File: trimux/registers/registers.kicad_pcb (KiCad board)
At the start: 2 copper layers, 50 x 50 mm, 36 parts, among them P1 CONN_02X05, U1 trimux, U2 trimux, U3 trimux, U4 trimux, U5 trimux, U6 trimux

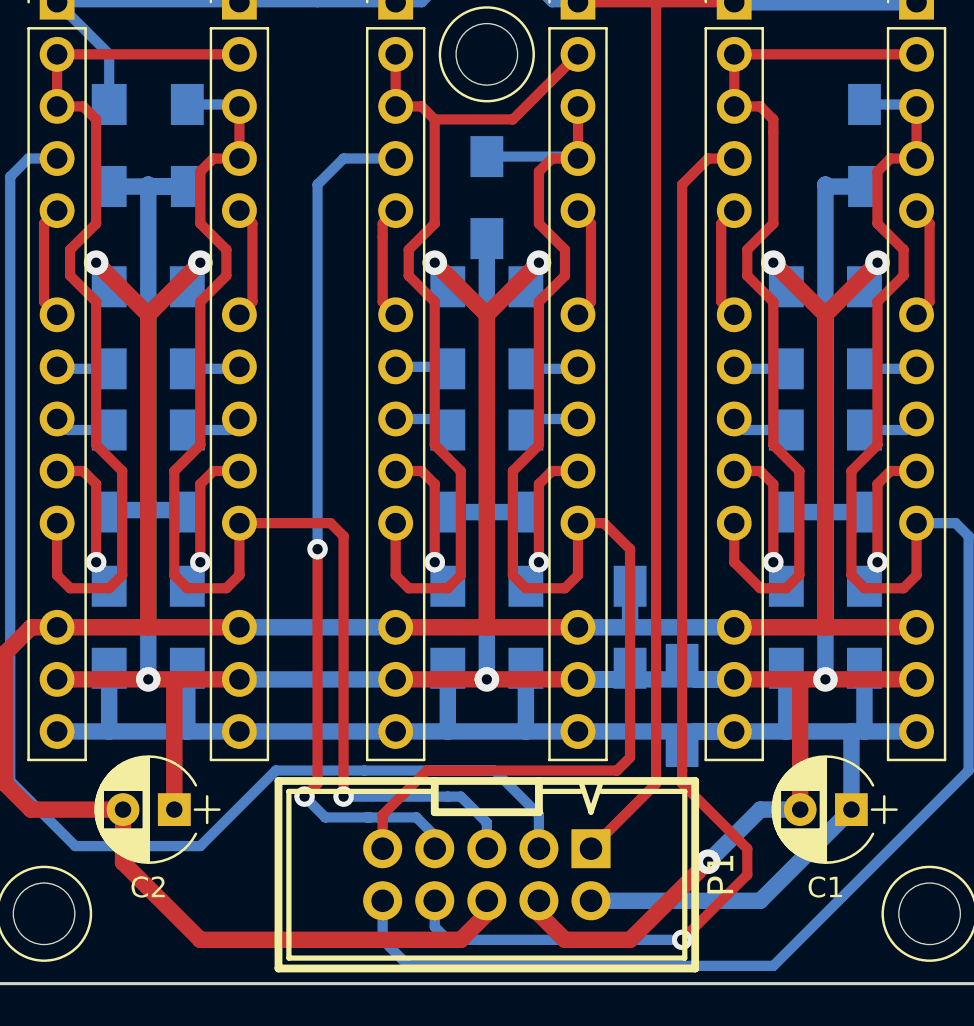
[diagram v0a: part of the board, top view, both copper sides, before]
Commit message: registers silkscreens
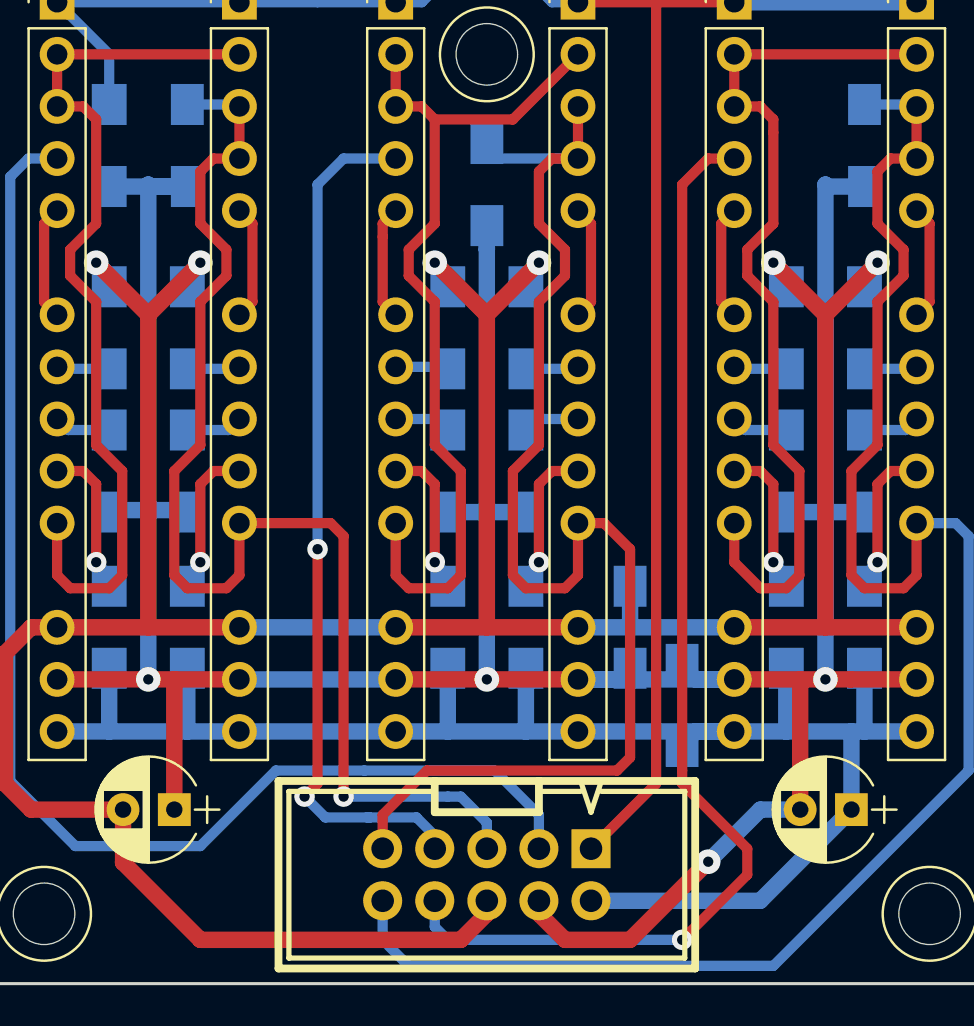
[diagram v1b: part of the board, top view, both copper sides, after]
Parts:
- moved C6 0.64 mm to (40.0, 26.0)
- renumbered REF** to 47uF
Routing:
- net GNDREF: track 166.0 -> 167.2 mm

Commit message: registers
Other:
- board text added: "+5"
- board text added: "-5"
- board text added: "0"
- board text added: "3-trit register"
- board text added: "Ahi"
- board text added: "Alo"
- board text added: "Ami"
- board text added: "CLK"
- board text added: "FlipFlapFlop high"
- board text added: "FlipFlapFlop low"
- board text added: "FlipFlapFlop mid"
- board text added: "Qhi"
- board text added: "Qlo"
- board text added: "Qmi"
- board text added: "this register stores 3-trit value on P-O-N clock fronts"
- board text added: "v25.09.2017"
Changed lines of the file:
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@@
-(kicad_pcb (version 4) (host pcbnew 4.0.5)
+(kicad_pcb (version 4) (host pcbnew 4.0.5+dfsg1-4)
   (general
     (links 103)
@@
     (area 14.924999 14.924999 65.075001 65.075001)
     (thickness 1.6)
-    (drawings 4)
+    (drawings 20)
     (tracks 381)
     (zones 0)
@@
     )
   )
+  (gr_text "this register stores 3-trit value\non P-O-N clock fronts" (at 48.26 34.925 90) (layer F.SilkS)
+    (effects (font (size 1.2 1.2) (thickness 0.2)))
+  )
+  (gr_text v25.09.2017 (at 63.754 21.336 90) (layer B.SilkS)
+    (effects (font (size 1.2 1.2) (thickness 0.3)) (justify mirror))
+  )
+  (gr_text "3-trit\nregister" (at 25.146 61.468) (layer F.SilkS)
+    (effects (font (size 1.2 1.2) (thickness 0.3)))
+  )
+  (gr_text CLK (at 46.99 56.388) (layer B.SilkS)
+    (effects (font (size 1.2 1.2) (thickness 0.3)) (justify mirror))
+  )
+  (gr_text Qhi (at 40.005 55.245) (layer B.SilkS)
+    (effects (font (size 1.2 1.2) (thickness 0.3)) (justify mirror))
+  )
+  (gr_text Ahi (at 42.545 56.515) (layer B.SilkS)
+    (effects (font (size 1.2 1.2) (thickness 0.3)) (justify mirror))
+  )
+  (gr_text Ami (at 36.83 56.515) (layer B.SilkS)
+    (effects (font (size 1.2 1.2) (thickness 0.3)) (justify mirror))
+  )
+  (gr_text Qmi (at 32.258 57.404) (layer B.SilkS)
+    (effects (font (size 1.2 1.2) (thickness 0.3)) (justify mirror))
+  )
+  (gr_text Qlo (at 32.512 62.23) (layer B.SilkS)
+    (effects (font (size 1.2 1.2) (thickness 0.3)) (justify mirror))
+  )
+  (gr_text Alo (at 36.83 62.992) (layer B.SilkS)
+    (effects (font (size 1.2 1.2) (thickness 0.3)) (justify mirror))
+  )
+  (gr_text -5 (at 40.64 62.992) (layer B.SilkS)
+    (effects (font (size 1.2 1.2) (thickness 0.3)) (justify mirror))
+  )
+  (gr_text 0 (at 43.18 62.992) (layer B.SilkS)
+    (effects (font (size 1.2 1.2) (thickness 0.3)) (justify mirror))
+  )
+  (gr_text +5 (at 47.498 62.484) (layer B.SilkS)
+    (effects (font (size 1.2 1.2) (thickness 0.3)) (justify mirror))
+  )
+  (gr_text "FlipFlapFlop mid" (at 40.005 38.1 90) (layer F.SilkS)
+    (effects (font (size 2.5 2.5) (thickness 0.3)))
+  )
+  (gr_text "FlipFlapFlop low" (at 56.515 34.925 90) (layer F.SilkS)
+    (effects (font (size 2.5 2.5) (thickness 0.3)))
+  )
+  (gr_text "FlipFlapFlop high" (at 23.495 34.925 90) (layer F.SilkS)
+    (effects (font (size 2.5 2.5) (thickness 0.3)))
+  )
   (gr_line (start 15 65) (end 15 15) (angle 90) (layer Edge.Cuts) (width 0.15))
   (gr_line (start 65 65) (end 15 65) (angle 90) (layer Edge.Cuts) (width 0.15))
@@
   (segment (start 21.59 52.705) (end 25.4 52.705) (width 0.8) (layer B.Cu) (net 1))
   (segment (start 25.4 52.705) (end 27.94 52.705) (width 0.8) (layer B.Cu) (net 1))
-  (segment (start 40.005 29.21) (end 40.005 28.035) (width 0.8) (layer B.Cu) (net 2) (status 800000))
+  (segment (start 40.005 29.21) (end 40.005 28.035) (width 0.8) (layer B.Cu) (net 2))
   (segment (start 35.56 50.165) (end 27.94 50.165) (width 0.8) (layer B.Cu) (net 2))
   (segment (start 42.545 61.595) (end 43.815 62.865) (width 0.8) (layer F.Cu) (net 2))
@@
   (segment (start 27.305 29.21) (end 27.305 29.21) (width 0.5) (layer F.Cu) (net 4))
   (segment (start 27.94 24.765) (end 27.94 22.225) (width 0.5) (layer F.Cu) (net 4))
-  (segment (start 40.005 24.035) (end 40.005 24.13) (width 0.5) (layer B.Cu) (net 5) (status C00000))
-  (segment (start 40.005 24.13) (end 40.64 24.765) (width 0.5) (layer B.Cu) (net 5) (status C00000))
-  (segment (start 40.64 24.765) (end 44.45 24.765) (width 0.5) (layer B.Cu) (net 5) (status C00000))
+  (segment (start 40.005 24.035) (end 40.005 24.13) (width 0.5) (layer B.Cu) (net 5))
+  (segment (start 40.005 24.13) (end 40.64 24.765) (width 0.5) (layer B.Cu) (net 5))
+  (segment (start 40.64 24.765) (end 44.45 24.765) (width 0.5) (layer B.Cu) (net 5))
   (segment (start 46.99 53.975) (end 46.355 54.61) (width 0.5) (layer F.Cu) (net 5))
   (segment (start 45.72 42.545) (end 46.99 43.815) (width 0.5) (layer F.Cu) (net 5))

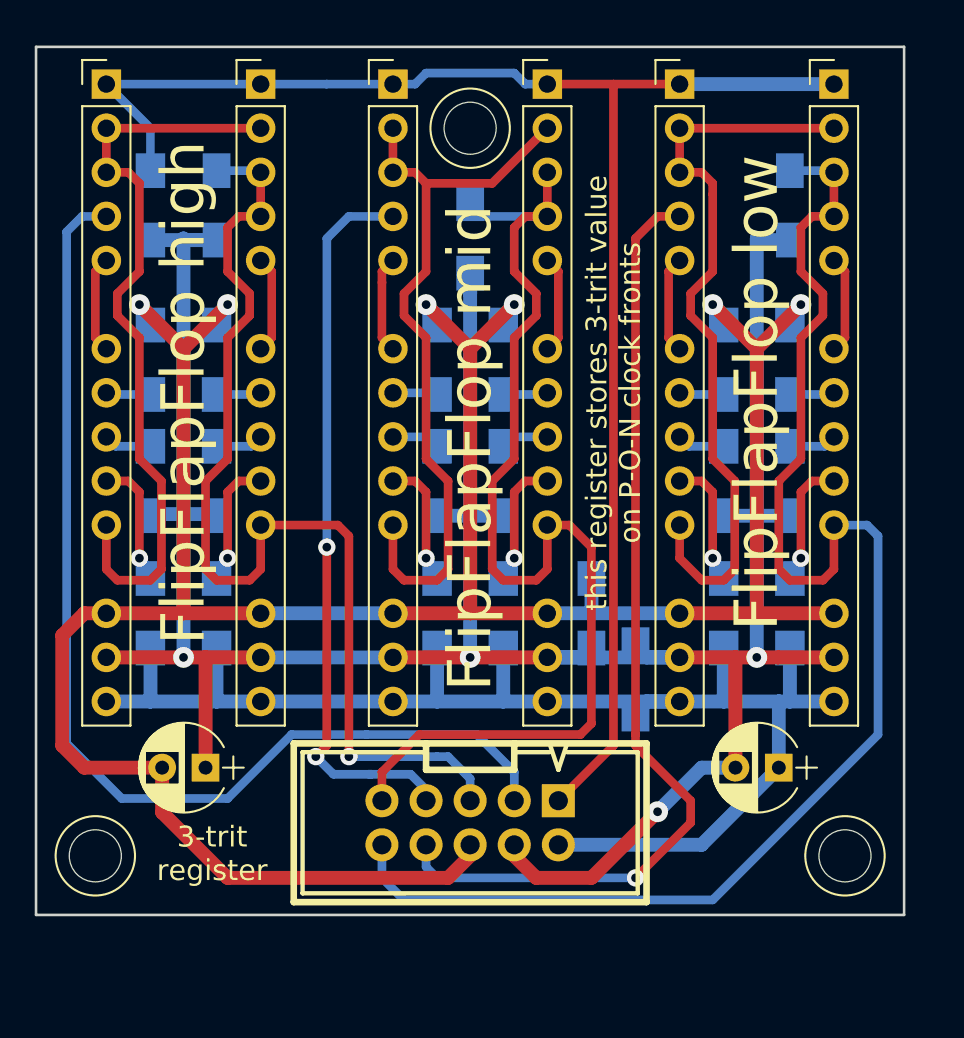
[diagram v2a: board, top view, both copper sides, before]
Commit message: leds for the flipflapflop register
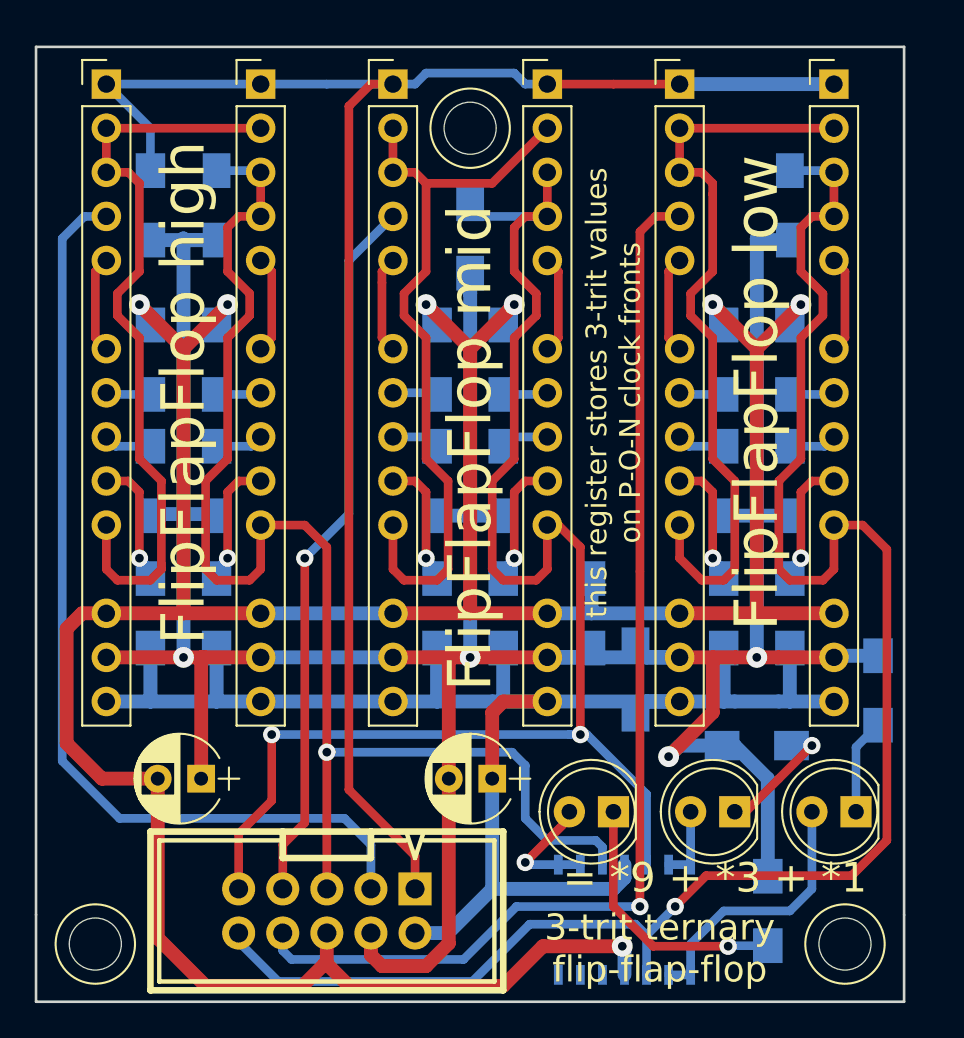
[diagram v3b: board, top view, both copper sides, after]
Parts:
- removed 47uF (x2): 1pin, Connectors:1pin
- added D1: LED_bicolor, LEDs:LED_D5.0mm, F.Cu at (48.3, 59.1)
- added D2: LED_bicolor, LEDs:LED_D5.0mm, F.Cu at (55.2, 59.1)
- added D3: LED_bicolor, LEDs:LED_D5.0mm, F.Cu at (62.2, 59.1)
- added R14: 330, Resistors_SMD:R_1206_HandSoldering, B.Cu at (57.1, 64.8)
- added R21: 330, Resistors_SMD:R_1206_HandSoldering, B.Cu at (56.5, 55.2)
- added R22: 330, Resistors_SMD:R_1206_HandSoldering, B.Cu at (63.5, 52.1)
- added REF**: 1pin, Connectors:1pin, F.Cu at (61.6, 66.7)
- added REF**: 1pin, Connectors:1pin, F.Cu at (18.4, 66.7)
- added U7: LM324, SMD_Packages:SOIC-14_N, B.Cu at (48.9, 65.4)
- moved C1 16.5 mm to (41.3, 57.1)
- moved P1 9.69 mm to (31.8, 64.8)
- moved C2 0.68 mm to (24.5, 57.1)
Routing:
- net GNDREF: track 167.2 -> 189.7 mm
- net /Qmi: track 65.4 -> 87.3 mm, vias 0 -> 2
- net -5V: track 159.9 -> 179.1 mm, vias 6 -> 7
- net /Qhi: track 62.3 -> 79.8 mm
- net /Qlo: track 84.0 -> 100.8 mm, vias 0 -> 1
- net Net-(D3-Pad2): track 0.00 -> 15.8 mm
- net Net-(D1-Pad1): track 0.00 -> 15.3 mm, vias 0 -> 1
- net +5V: track 81.6 -> 91.0 mm
- net /Alo: track 56.1 -> 64.6 mm
- net /Ahi: track 63.3 -> 55.5 mm
- net Net-(D1-Pad2): track 0.00 -> 7.20 mm, vias 0 -> 1
- net Net-(D2-Pad1): track 0.00 -> 7.20 mm, vias 0 -> 1
- net /CLK: track 91.1 -> 98.2 mm
- net Net-(D3-Pad1): track 0.00 -> 5.51 mm
- net Net-(D2-Pad2): track 0.00 -> 4.32 mm
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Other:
- board size 50 x 50 mm -> 50 x 55 mm
- board text added: "3-trit ternary flip-flap-flop"
- board text added: "= *9 + *3 + *1"
- board text added: "this register stores 3-trit values on P-O-N clock fronts"
- board text added: "v26.09.2017"
- board text removed: "3-trit register"
- board text removed: "this register stores 3-trit value on P-O-N clock fronts"
- board text removed: "v25.09.2017"

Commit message: memory
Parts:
- added C10: 47u, Capacitors_THT:CP_Radial_D5.0mm_P2.50mm, F.Cu at (27.3, 109.2)
- added C11: 47u, Capacitors_THT:CP_Radial_D5.0mm_P2.50mm, F.Cu at (45.1, 106.7)
- added C8: 104, Capacitors_SMD:C_1206_HandSoldering, B.Cu at (34.9, 108.6)
- added C9: 104, Capacitors_SMD:C_1206_HandSoldering, B.Cu at (37.5, 105.4)
- added NPTH4: 1pin, Connectors:1pin, F.Cu at (18.4, 73.0)
- added NPTH5: 1pin, Connectors:1pin, F.Cu at (61.6, 73.0)
- added NPTH6: 1pin, Connectors:1pin, F.Cu at (61.6, 111.8)
- added NPTH7: 1pin, Connectors:1pin, F.Cu at (18.4, 111.8)
- added P2: CONN_02X08, registers:IDC16, F.Cu at (59.7, 91.4)
- added P3: CONN_01X04, Pin_Headers:Pin_Header_Straight_1x04_Pitch2.54mm, F.Cu at (17.8, 87.6)
- added R23: 150, Resistors_SMD:R_1206_HandSoldering, B.Cu at (25.9, 90.8)
- added R24: 150, Resistors_SMD:R_1206_HandSoldering, B.Cu at (28.6, 97.7)
- added R25: 150, Resistors_SMD:R_1206_HandSoldering, B.Cu at (25.9, 100.3)
- added U10: trimux, trimux:trimux1x15_2.54, F.Cu at (31.8, 73.7)
- added U12: trimux, trimux:trimux1x15_2.54, F.Cu at (22.9, 73.7)
- added U8: trimux, trimux:trimux1x15_2.54, F.Cu at (49.5, 73.7)
- added U9: trimux, trimux:trimux1x15_2.54, F.Cu at (40.6, 73.7)
- moved NPTH1 0.51 mm to (40.0, 19.2)
- moved C2 0.38 mm to (24.1, 57.1)
- moved C1 0.13 mm to (41.1, 57.1)
- renumbered REF** to NPTH1, REF** to NPTH2, REF** to NPTH3
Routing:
- net GNDREF: track 189.7 -> 263.5 mm, vias 4 -> 0
- net /LO: track 0.00 -> 71.6 mm
- net -5V: track 179.1 -> 241.9 mm, vias 7 -> 1
- net +5V: track 91.0 -> 150.8 mm
- net Net-(P2-Pad10): track 0.00 -> 54.3 mm
- net Net-(P2-Pad6): track 0.00 -> 52.7 mm
- net Net-(P2-Pad12): track 0.00 -> 48.5 mm, vias 0 -> 1
- net Net-(P2-Pad8): track 0.00 -> 41.8 mm
- net Net-(U10-Pad4): track 0.00 -> 41.7 mm
- net Net-(P2-Pad1): track 0.00 -> 35.9 mm
- net /MI: track 0.00 -> 33.0 mm
- net Net-(P2-Pad9): track 0.00 -> 29.0 mm, vias 0 -> 1
- net Net-(U10-Pad8): track 0.00 -> 28.6 mm
- net Net-(P2-Pad11): track 0.00 -> 22.7 mm
- net Net-(U10-Pad11): track 0.00 -> 21.5 mm
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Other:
- board outline removed
- board text added: "1"
- board text added: "12"
- board text added: "13"
- board text added: "1:13 ternary multiplexer"
- board text added: "2"
- board text added: "3"
- board text added: "C/A/Q"
- board text added: "GND"
- board text added: "HI"
- board text added: "LO"
- board text added: "MI"

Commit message: memory
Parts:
- added C12: 104, Capacitors_SMD:C_1206_HandSoldering, B.Cu at (16.5, 22.2)
- added C13: 104, Capacitors_SMD:C_1206_HandSoldering, B.Cu at (38.7, 26.0)
- added C14: 104, Capacitors_SMD:C_1206_HandSoldering, B.Cu at (55.2, 24.1)
- added C15: 104, Capacitors_SMD:C_1206_HandSoldering, B.Cu at (75.7, 107.2)
- added C16: 104, Capacitors_SMD:C_1206_HandSoldering, B.Cu at (69.6, 104.1)
- added C17: 47u, Capacitors_THT:CP_Radial_D5.0mm_P2.00mm, F.Cu at (85.3, 111.8)
- added C18: 47u, Capacitors_THT:CP_Radial_D5.0mm_P2.00mm, F.Cu at (76.2, 111.8)
- added C19: 104, Capacitors_SMD:C_1206_HandSoldering, B.Cu at (78.2, 83.8)
- added C20: 104, Capacitors_SMD:C_1206_HandSoldering, B.Cu at (88.4, 83.3)
- added D4: LED_bicolor, LEDs:LED_D5.0mm, F.Cu at (102.1, 85.9)
- added D5: LED_bicolor, LEDs:LED_D5.0mm, F.Cu at (102.1, 92.5)
- added D6: LED_bicolor, LEDs:LED_D5.0mm, F.Cu at (102.1, 99.1)
- added J1: Conn_01x01, Pin_Headers:Pin_Header_Straight_1x01_Pitch2.54mm, F.Cu at (112.3, 79.2)
- added NPTH5: 1pin, Connectors:1pin, F.Cu at (111.9, 73.0)
- added NPTH5: 1pin, Connectors:1pin, F.Cu at (111.9, 111.6)
- added NPTH5: 1pin, Connectors:1pin, F.Cu at (68.2, 111.6)
- added NPTH5: 1pin, Connectors:1pin, F.Cu at (68.2, 73.0)
- added P4: CONN_02X05, registers:IDC10, F.Cu at (109.2, 93.0)
- added R26: 150, Resistors_SMD:R_1206_HandSoldering, B.Cu at (69.6, 97.5)
- added R27: 150, Resistors_SMD:R_1206_HandSoldering, B.Cu at (75.2, 92.5)
- added R28: 150, Resistors_SMD:R_1206_HandSoldering, B.Cu at (79.2, 99.1)
- added R29: 150, Resistors_SMD:R_1206_HandSoldering, B.Cu at (79.2, 91.9)
- added R30: 10k, Resistors_SMD:R_1206_HandSoldering, B.Cu at (88.4, 75.2)
- added R31: 150, Resistors_SMD:R_1206_HandSoldering, B.Cu at (84.3, 91.9)
- added R32: 150, Resistors_SMD:R_1206_HandSoldering, B.Cu at (88.4, 91.9)
- added R33: 150, Resistors_SMD:R_1206_HandSoldering, B.Cu at (88.4, 99.6)
- added R34: 330, Resistors_SMD:R_1206_HandSoldering, B.Cu at (101.1, 82.8)
- added R35: 330, Resistors_SMD:R_1206_HandSoldering, B.Cu at (101.1, 89.4)
- added R36: 330, Resistors_SMD:R_1206_HandSoldering, B.Cu at (101.1, 95.5)
- added U11: trimux, trimux:trimux1x15_2.54, F.Cu at (72.6, 74.2)
- added U13: trimux, trimux:trimux1x15_2.54, F.Cu at (81.8, 74.2)
- added U14: trimux, trimux:trimux1x15_2.54, F.Cu at (90.9, 74.2)
- added U15: LM324, SMD_Packages:SOIC-14_N, B.Cu at (103.1, 107.2)
- moved C6 1.27 mm to (41.3, 26.0)
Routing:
- net GNDREF: track 263.5 -> 276.8 mm
- net Net-(C13-Pad1): track 33.4 -> 37.3 mm
- net Net-(C14-Pad1): track 33.7 -> 36.9 mm
- net Net-(C12-Pad1): track 33.5 -> 36.3 mm
- net /Qmi: track 74.2 -> 73.2 mm

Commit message: memory board
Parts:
- removed C15, C16, C19, C20: 104, Capacitors_SMD:C_1206_HandSoldering
- removed C17, C18: 47u, Capacitors_THT:CP_Radial_D5.0mm_P2.00mm
- removed D4, D5, D6: LED_bicolor, LEDs:LED_D5.0mm
- removed J1: Conn_01x01, Pin_Headers:Pin_Header_Straight_1x01_Pitch2.54mm
- removed the NPTH5 at (111.9, 73.0)
- removed the NPTH5 at (111.9, 111.6)
- removed the NPTH5 at (68.2, 111.6)
- removed the NPTH5 at (68.2, 73.0)
- removed R26, R27, R28, R29, R31, R32, R33: 150, Resistors_SMD:R_1206_HandSoldering
- removed R30: 10k, Resistors_SMD:R_1206_HandSoldering
- removed R34, R35, R36: 330, Resistors_SMD:R_1206_HandSoldering
- removed U11, U13, U14: trimux, trimux:trimux1x15_2.54
- removed U15: LM324, SMD_Packages:SOIC-14_N
- added P5: CONN_01X02, Pin_Headers:Pin_Header_Straight_1x02_Pitch1.27mm, F.Cu at (30.1, 45.3)
- added P6: CONN_01X02, Pin_Headers:Pin_Header_Straight_1x02_Pitch1.27mm, F.Cu at (32.5, 23.0)
- added P7: CONN_01X02, Pin_Headers:Pin_Header_Straight_1x02_Pitch1.27mm, F.Cu at (49.3, 42.7)
- added P8: CONN_01X02, Pin_Headers:Pin_Header_Straight_1x02_Pitch1.27mm, F.Cu at (47.2, 26.0)
- added P9: CONN_01X02, Pin_Headers:Pin_Header_Straight_1x02_Pitch1.27mm, F.Cu at (63.5, 29.0)
- P4: value CONN_02X05 -> CONN_01X02; footprint registers:IDC10 -> Pin_Headers:Pin_Header_Straight_1x02_Pitch1.27mm
- moved P4 107.5 mm to (23.0, 28.7), turned to 90 degrees
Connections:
- P4 pad 1: /CLK -> Net-(P4-Pad1)
- P4 pad 2: +5V -> Net-(C12-Pad1)
- U1 pad 11: Net-(C12-Pad1) -> Net-(P4-Pad1)
- U2 pad 11: /Qhi -> Net-(P5-Pad1)
- U3 pad 11: Net-(C13-Pad1) -> Net-(P6-Pad1)
- U4 pad 11: /Qmi -> Net-(P8-Pad1)
- U5 pad 11: Net-(C14-Pad1) -> Net-(P7-Pad1)
- U6 pad 11: /Qlo -> Net-(P9-Pad1)
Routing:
- net Net-(P6-Pad1): track 0.00 -> 20.8 mm, vias 0 -> 1
- net Net-(P8-Pad1): track 0.00 -> 18.1 mm
- net Net-(P4-Pad1): track 0.00 -> 17.2 mm
- net Net-(C13-Pad1): track 37.3 -> 21.8 mm
- net Net-(P9-Pad1): track 0.00 -> 14.9 mm
- net Net-(C12-Pad1): track 36.3 -> 22.7 mm
- net -5V: track 241.9 -> 228.6 mm
- net /Qmi: track 73.2 -> 78.8 mm
- net /Qlo: track 88.2 -> 93.5 mm
- net Net-(C14-Pad1): track 36.9 -> 42.2 mm
- net Net-(P5-Pad1): track 0.00 -> 4.96 mm
- net Net-(P7-Pad1): track 0.00 -> 4.37 mm
- net /Ami: track 42.2 -> 44.7 mm
- net /CLK: track 96.6 -> 97.8 mm
- net /Qhi: track 72.7 -> 71.9 mm
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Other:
- board text added: "Cut 6 QN jumpers to insert initializers"
- board text added: "QN"
